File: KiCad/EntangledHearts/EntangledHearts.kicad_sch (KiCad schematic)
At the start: 60 parts, among them J1 OLED Display, J2 MPU, J3 USB4135-GF-A, Q1 SFH_3711, Q3 2N7002, Q4 2N7002, U1 ESP32-S3-WROOM-1, U2 MCP73831-2-OT, U3 TC1185-xCT

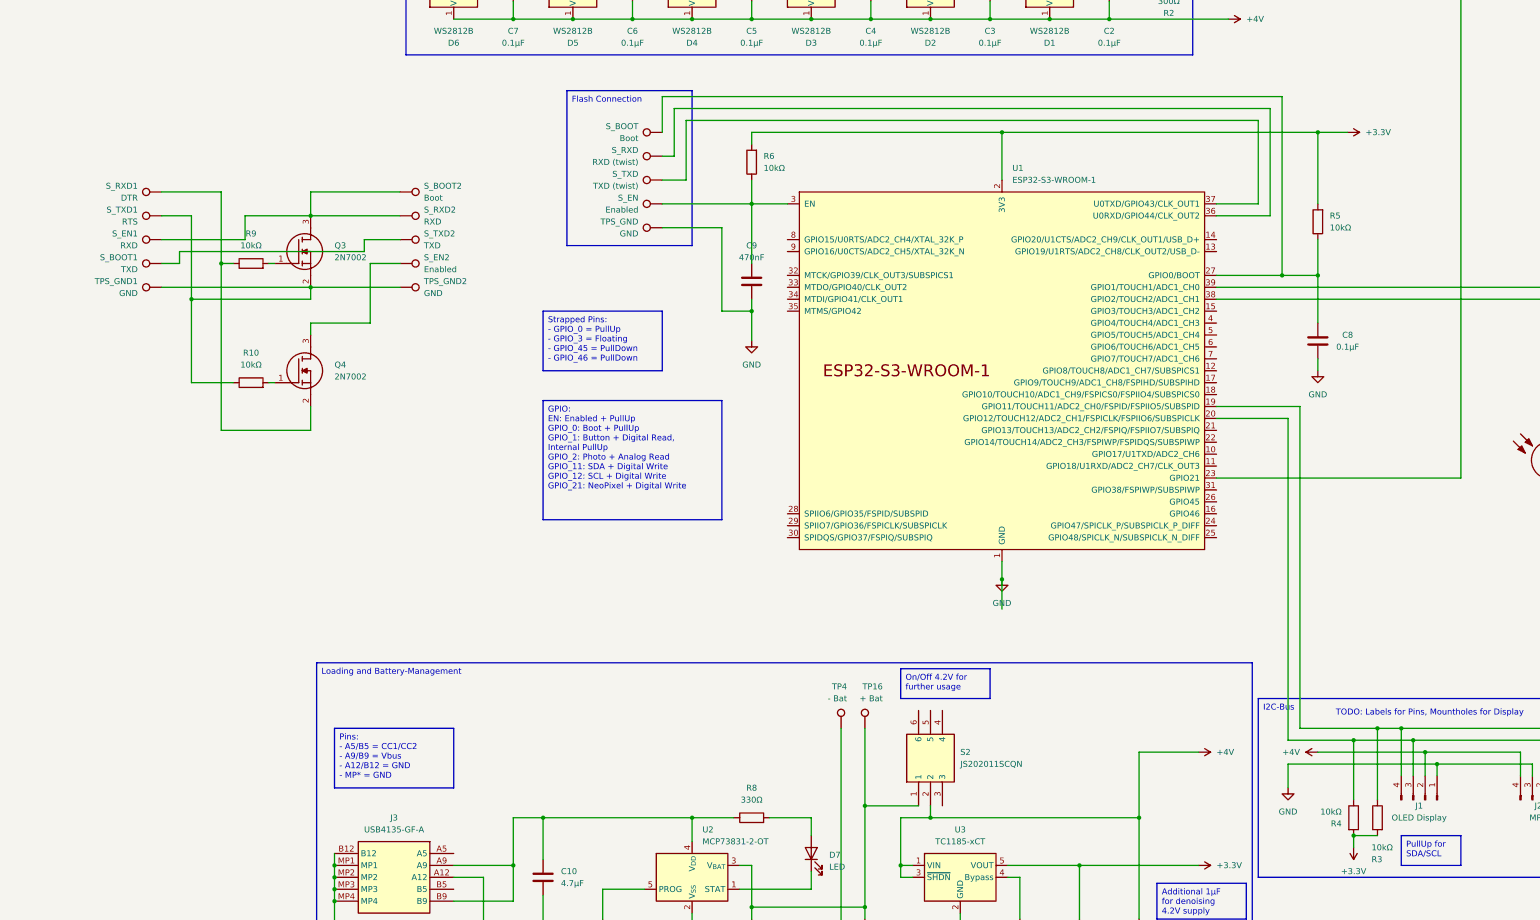
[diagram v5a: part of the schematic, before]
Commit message: ADD: all footprints added
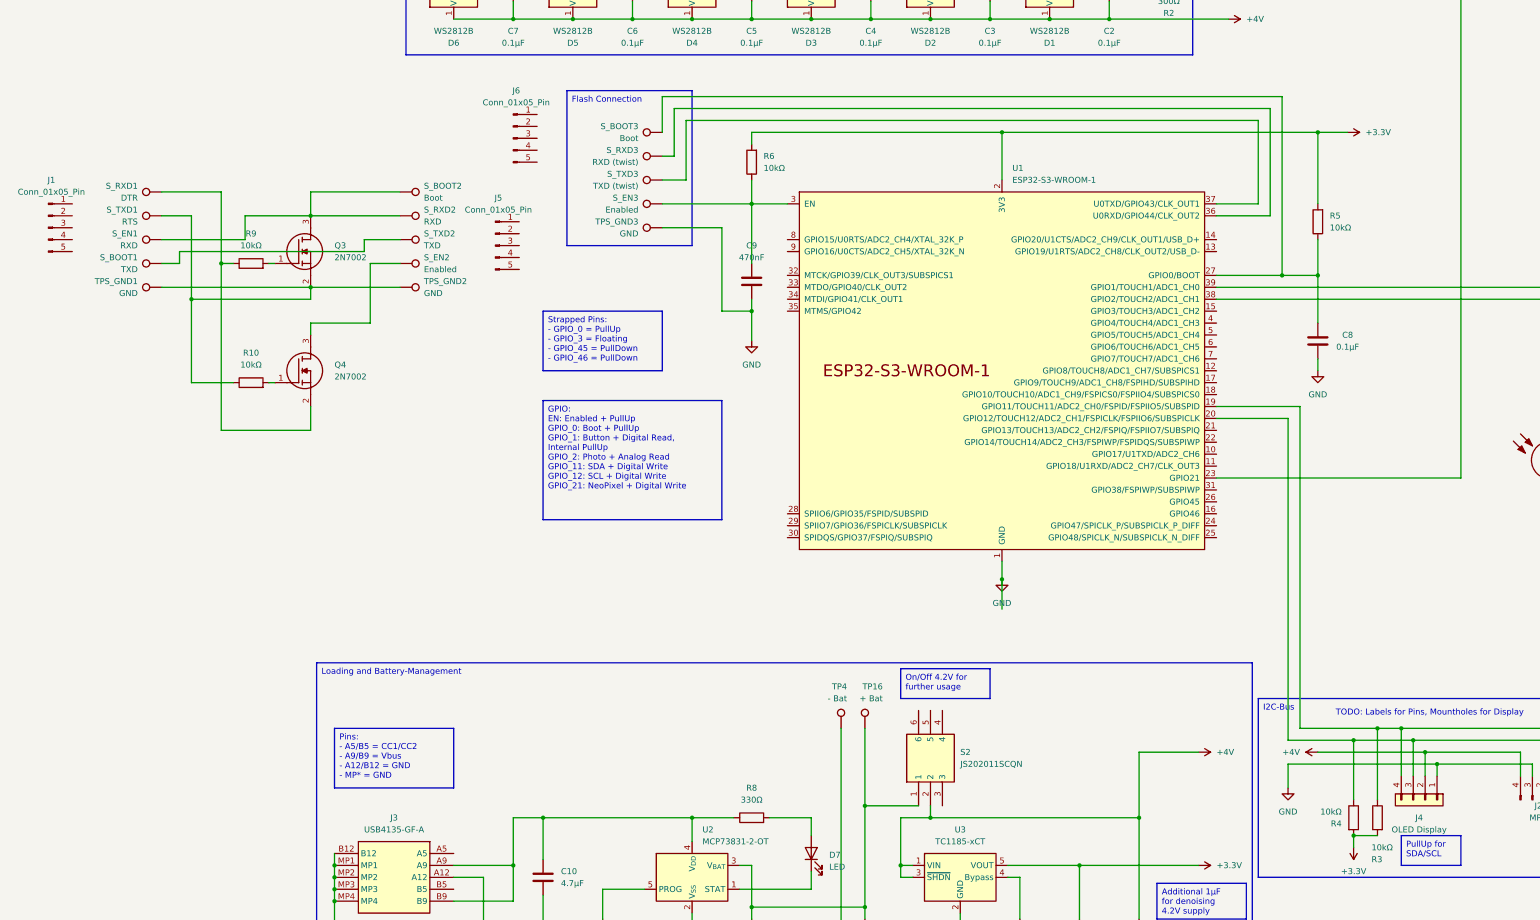
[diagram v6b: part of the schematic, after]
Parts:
- removed J1: OLED Display, symbol Connector:Conn_01x04_Pin
- added J1, J5, J6: Conn_01x05_Pin, Connector_PinHeader_2.54mm:PinHeader_1x05_P2.54mm_Vertical_SMD_Pin1Left, symbol Connector:Conn_01x05_Pin
- added J4: OLED Display, Connector_PinHeader_2.54mm:PinHeader_1x04_P2.54mm_Vertical, symbol Connector_Generic:Conn_01x04
- C10, C11, C12, C13, C14, C15: footprint (none) -> Capacitor_SMD:C_0805_2012Metric
- D7: footprint (none) -> LED_SMD:LED_0805_2012Metric
- J2: footprint (none) -> Connector_PinHeader_2.54mm:PinHeader_1x04_P2.54mm_Vertical_SMD_Pin1Left
- R1, R2, R3, R4, R5, R6, R7, R8: footprint (none) -> Resistor_SMD:R_0805_2012Metric
- S_BOOT1, S_BOOT2, S_EN1, S_EN2, S_RXD1, S_RXD2, S_TXD1, S_TXD2, TP16, TP4, TPS_GND1, TPS_GND2: footprint (none) -> TestPoint:TestPoint_Pad_1.0x1.0mm
- S_BOOT3: renamed from S_BOOT; footprint (none) -> TestPoint:TestPoint_Pad_1.0x1.0mm
- S_EN3: renamed from S_EN; footprint (none) -> TestPoint:TestPoint_Pad_1.0x1.0mm
- S_RXD3: renamed from S_RXD; footprint (none) -> TestPoint:TestPoint_Pad_1.0x1.0mm
- S_TXD3: renamed from S_TXD; footprint (none) -> TestPoint:TestPoint_Pad_1.0x1.0mm
- TPS_GND3: renamed from TPS_GND; footprint (none) -> TestPoint:TestPoint_Pad_1.0x1.0mm
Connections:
- net +4V: now also J4.2 (Pin_2)
- net GND: now also J4.1 (Pin_1)
- net at J2.2 (Pin_2), R4.1, U1.20 (GPIO12/TOUCH12/ADC2_CH1/FSPICLK/FSPIIO6/SUBSPICLK): now also J4.3 (Pin_3)
- net at J2.1 (Pin_1), R3.1, U1.19 (GPIO11/TOUCH11/ADC2_CH0/FSPID/FSPIIO5/SUBSPID): now also J4.4 (Pin_4)

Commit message: ADD: first pcbs added
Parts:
- removed S_BOOT1, S_TXD2: TXD, TestPoint:TestPoint_Pad_1.0x1.0mm, symbol Connector:TestPoint
- removed S_BOOT2, S_BOOT3: Boot, TestPoint:TestPoint_Pad_1.0x1.0mm, symbol Connector:TestPoint
- removed S_EN1, S_RXD2: RXD, TestPoint:TestPoint_Pad_1.0x1.0mm, symbol Connector:TestPoint
- removed S_EN2, S_EN3: Enabled, TestPoint:TestPoint_Pad_1.0x1.0mm, symbol Connector:TestPoint
- removed S_RXD1: DTR, TestPoint:TestPoint_Pad_1.0x1.0mm, symbol Connector:TestPoint
- removed S_RXD3: RXD (twist), TestPoint:TestPoint_Pad_1.0x1.0mm, symbol Connector:TestPoint
- removed S_TXD1: RTS, TestPoint:TestPoint_Pad_1.0x1.0mm, symbol Connector:TestPoint
- removed S_TXD3: TXD (twist), TestPoint:TestPoint_Pad_1.0x1.0mm, symbol Connector:TestPoint
- removed TPS_GND1, TPS_GND2, TPS_GND3: GND, TestPoint:TestPoint_Pad_1.0x1.0mm, symbol Connector:TestPoint
- +Bat1: renamed from TP16; footprint TestPoint:TestPoint_Pad_1.0x1.0mm -> TestPoint:TestPoint_Pad_2.5x2.5mm
- -Bat1: renamed from TP4; footprint TestPoint:TestPoint_Pad_1.0x1.0mm -> TestPoint:TestPoint_Pad_2.5x2.5mm
- Seriell_Flash1: renamed from J6; value Conn_01x05_Pin -> Flash
- Seriell_Input1: renamed from J1; value Conn_01x05_Pin -> Input
- Seriell_Output1: renamed from J5; value Conn_01x05_Pin -> Output
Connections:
- net GND: now also Seriell_Flash1.5 (Pin_5)
- net at Seriell_Flash1.1 (Pin_1): now also C8.2, R5.1, U1.27 (GPIO0/BOOT)
- net at Seriell_Flash1.2 (Pin_2): now also U1.36 (U0RXD/GPIO44/CLK_OUT2)
- net at Seriell_Flash1.3 (Pin_3): now also U1.37 (U0TXD/GPIO43/CLK_OUT1)
- net at Seriell_Flash1.4 (Pin_4): now also C9.2, R6.1, U1.3 (EN)
- net at Q4.3 (D): now also Seriell_Output1.4 (Pin_4)
- net at Q3.3 (D): now also Seriell_Output1.1 (Pin_1)
- net at Q4.2 (S), R9.1: now also Seriell_Input1.1 (Pin_1)
- net at Q3.2 (S), R10.1: now also Seriell_Input1.2 (Pin_2)
- net at Seriell_Output1.2 (Pin_2): now also Seriell_Input1.3 (Pin_3)
- net at Seriell_Output1.3 (Pin_3): now also Seriell_Input1.4 (Pin_4)
- net at Seriell_Output1.5 (Pin_5): now also Seriell_Input1.5 (Pin_5)
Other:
- note added: "Boot"
- note added: "DTR"
- note added: "EN"
- note added: "GND"
- note added: "RTS"
- note added: "RXD"
- note added: "TODO: Labels for Pins"
- note added: "TXD"
- note removed: "TODO: Labels for Pins, Mountholes for Display"

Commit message: CHG cleanup of Schematics done
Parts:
- removed J2: MPU, Connector_PinHeader_2.54mm:PinHeader_1x04_P2.54mm_Vertical_SMD_Pin1Left, symbol Connector:Conn_01x04_Pin
- removed R3, R4: 10kΩ, Resistor_SMD:R_0805_2012Metric, symbol Device:R
- added ButtonA1: ButtonA1, TestPoint:TestPoint_Pad_1.5x1.5mm, symbol Connector:TestPoint
- added ButtonA2: ButtonA2, TestPoint:TestPoint_Pad_1.5x1.5mm, symbol Connector:TestPoint
- added ButtonB1: ButtonB1, TestPoint:TestPoint_Pad_1.5x1.5mm, symbol Connector:TestPoint
- added ButtonB2: ButtonB2, TestPoint:TestPoint_Pad_1.5x1.5mm, symbol Connector:TestPoint
- added MPU1: Conn_01x08_Pin, Connector_PinHeader_2.54mm:PinHeader_1x08_P2.54mm_Vertical_SMD_Pin1Left, symbol Connector:Conn_01x08_Pin
- added PU_SCL1, PU_SDA1: 10kΩ, Resistor_SMD:R_0805_2012Metric, symbol Device:R
- added PhotoA1: PhotoA1, TestPoint:TestPoint_Pad_1.5x1.5mm, symbol Connector:TestPoint
- added PhotoA2: PhotoA2, TestPoint:TestPoint_Pad_1.5x1.5mm, symbol Connector:TestPoint
- added PhotoB1: PhotoB1, TestPoint:TestPoint_Pad_1.5x1.5mm, symbol Connector:TestPoint
- added PhotoB2: PhotoB2, TestPoint:TestPoint_Pad_1.5x1.5mm, symbol Connector:TestPoint
- D1: value WS2812B -> NP1
- D2: value WS2812B -> NP2
- D3: value WS2812B -> NP3
- D4: value WS2812B -> NP4
- D5: value WS2812B -> NP5
- D6: value WS2812B -> NP6
- renumbered U3 to BM1, S1 to Button1, C11 to CP2, C12 to CP3, C13 to CP4, C15 to CP5, C14 to CP6, C10 to CP_CP1, C8 to C_Boot1, C1 to C_Button1, C9 to C_EN1, C2 to C_NP1, C3 to C_NP2, C4 to C_NP3, C5 to C_NP4, C6 to C_NP5, C7 to C_NP6, J4 to Display1, U1 to ESP1, D7 to LED1, R7 to PD_Prog1, U2 to PM1, R5 to PU_Boot1, R6 to PU_EN1, R1 to PU_Photo1, Q1 to Photo1, S2 to PowerSwitch1, Q3 to Q_BOOT1, Q4 to Q_EN1, R9 to R_DTR1, R8 to R_LED1, R2 to R_NP1, R10 to R_RTS1, J3 to USB1
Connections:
- net +3.3V: now also PU_SCL1.2, PU_SDA1.2; no longer PU_Photo1.2
- net +4V: now also Display1.3 (Pin_3), MPU1.1 (Pin_1); no longer Display1.2 (Pin_2)
- net GND: now also Display1.4 (Pin_4), ButtonB1.1, MPU1.2 (Pin_2), PhotoB1.1; no longer Button1.3, Display1.1 (Pin_1), Photo1.1 (E)
- net Boot: now reaches C_Boot1.2, ESP1.27 (GPIO0/BOOT), PU_Boot1.1, Seriell_Flash1.1 (Pin_1)
- net RXD: now reaches Seriell_Flash1.2 (Pin_2)
- net RXD: now also ESP1.37 (U0TXD/GPIO43/CLK_OUT1); no longer ESP1.36 (U0RXD/GPIO44/CLK_OUT2)
- net TXD: now reaches Seriell_Flash1.3 (Pin_3)
- net TXD: now also ESP1.36 (U0RXD/GPIO44/CLK_OUT2); no longer ESP1.37 (U0TXD/GPIO43/CLK_OUT1)
- net EN: now reaches C_EN1.2, ESP1.3 (EN), PU_EN1.1, Seriell_Flash1.4 (Pin_4)
- net Photo: now reaches ESP1.38 (GPIO2/TOUCH2/ADC1_CH1), PU_Photo1.1
- net Photo: now also PhotoA1.1; no longer Photo1.2 (C)
- net SDA: now reaches ESP1.20 (GPIO12/TOUCH12/ADC2_CH1/FSPICLK/FSPIIO6/SUBSPICLK)
- net SDA: now also Display1.1 (Pin_1), MPU1.4 (Pin_4), PU_SDA1.1; no longer Display1.3 (Pin_3)
- net SCL: now reaches ESP1.19 (GPIO11/TOUCH11/ADC2_CH0/FSPID/FSPIIO5/SUBSPID)
- net SCL: now also Display1.2 (Pin_2), MPU1.3 (Pin_3), PU_SCL1.1; no longer Display1.4 (Pin_4)
- net NeoPixel: now reaches ESP1.23 (GPIO21), R_NP1.1
- net Button: now reaches C_Button1.1, ESP1.39 (GPIO1/TOUCH1/ADC1_CH0)
- net Button: now also ButtonA1.1; no longer Button1.4
- new net: Photo1.2 (C), PhotoA2.1
- new net: Button1.4, ButtonA2.1
- new net: Button1.3, ButtonB2.1
- new net: Photo1.1 (E), PhotoB2.1
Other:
- note added: "SCL"
- note added: "SDA"
- note added: "VCC"
- note removed: "Internal PullUp"
- note removed: "TODO: Labels for Pins"
- moved on the sheet: +Bat1, -Bat1, BM1, Button1, CP2, CP3, CP4, CP5, CP6, CP_CP1, C_Boot1, C_Button1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
